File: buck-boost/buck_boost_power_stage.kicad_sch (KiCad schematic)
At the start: 27 parts, among them K1 Relay_SPDT, K2 Relay_SPDT, Q1 Q_NMOS_GDS, Q2 Q_NMOS_GDS, Q3 Q_NMOS_GDS, Q4 Q_NMOS_GDS, Q5 Q_NMOS_GDS

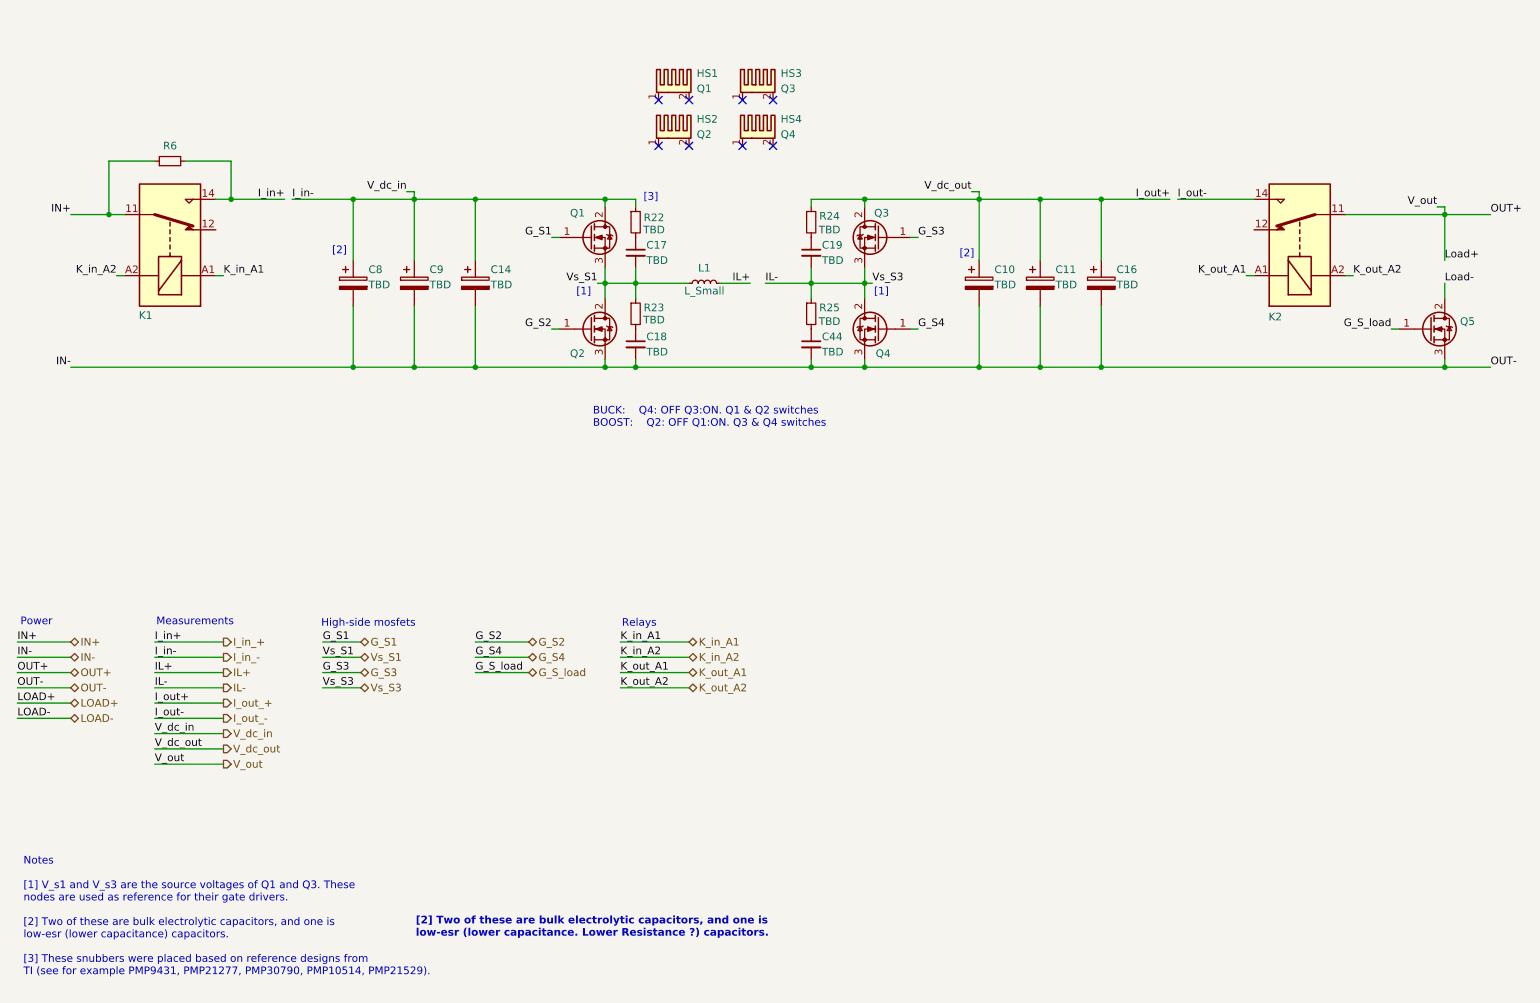
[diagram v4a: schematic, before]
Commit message: Editing sheets(Power labels, sheet color, adding text), Adding information in the sensor sheets
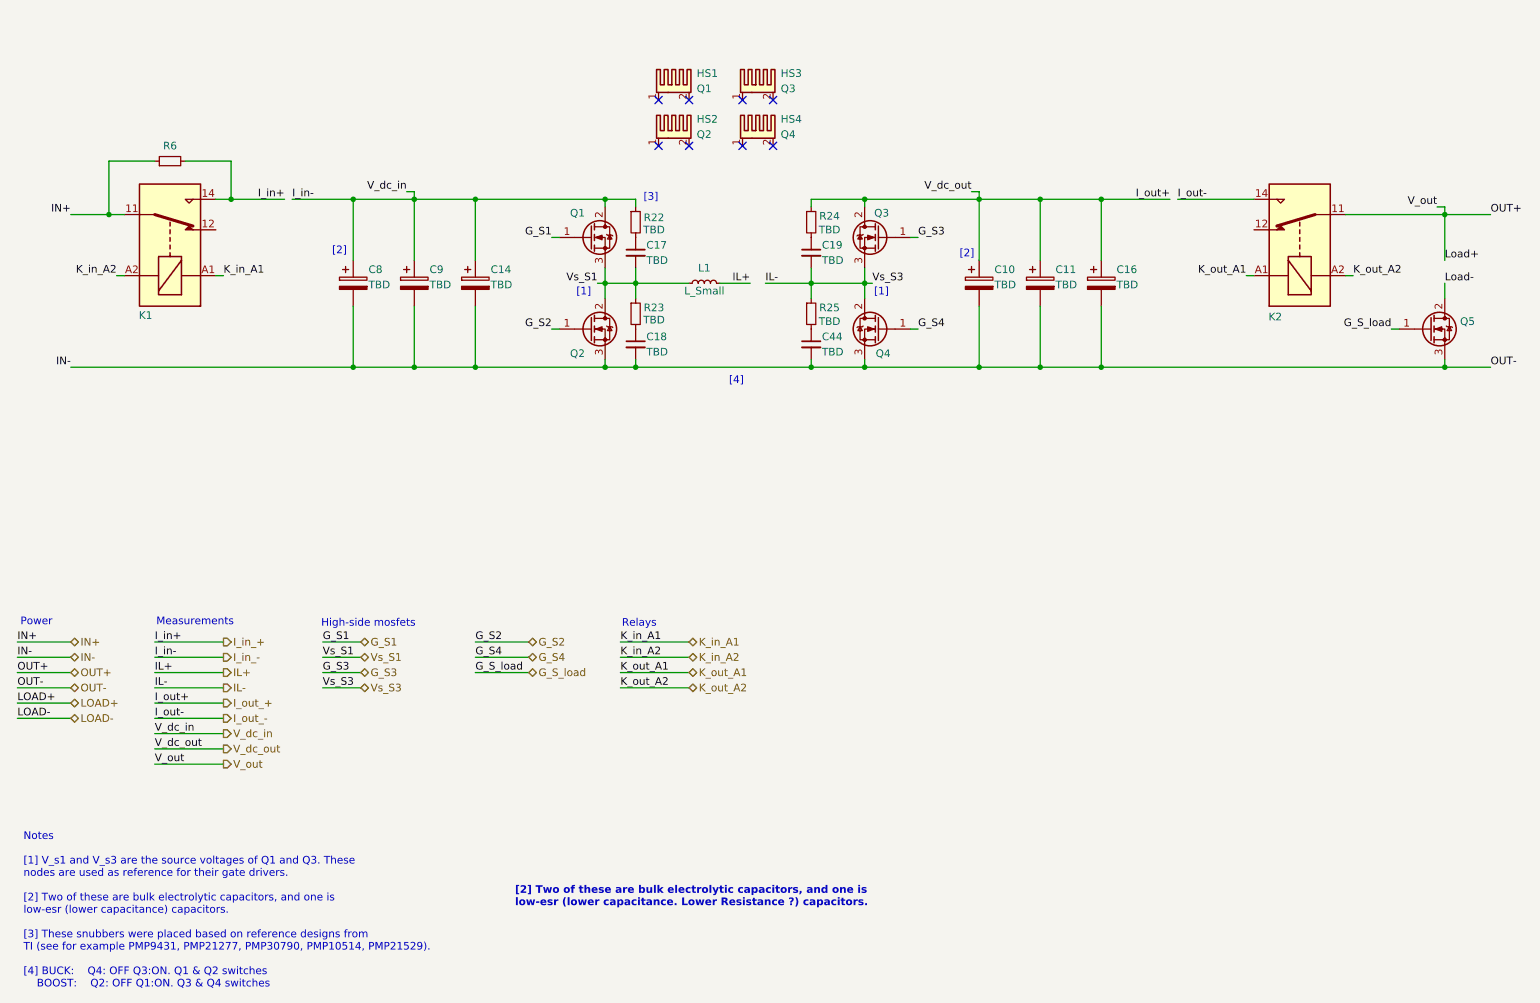
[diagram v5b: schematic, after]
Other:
- note added: "Notes [1] V_s1 and V_s3 are the source voltages of Q1 and Q3. These nodes are used as reference for their gate drivers. [2] Two of these are bulk electrolytic capacitors, and one is low-esr (lower capacitance) capacitors. [3] These snubbers were placed based on reference designs from TI (see for example PMP9431, PMP21277, PMP30790, PMP10514, PMP21529). [4] BUCK: Q4: OFF Q3:ON. Q1 & Q2 switches BO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"
- note added: "[4]"
- note removed: "BUCK: Q4: OFF Q3:ON. Q1 & Q2 switches BOOST: Q2: OFF Q1:ON. Q3 & Q4 switches"
- note removed: "Notes [1] V_s1 and V_s3 are the source voltages of Q1 and Q3. These nodes are used as reference for their gate drivers. [2] Two of these are bulk electrolytic capacitors, and one is low-esr (lower capacitance) capacitors. [3] These snubbers were placed based on reference designs from TI (see for example PMP9431, PMP21277, PMP30790, PMP10514, PMP21529)."
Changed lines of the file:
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@@
 		)
 	)
-	(text "BUCK:	Q4: OFF Q3:ON. Q1 & Q2 switches\nBOOST:	Q2: OFF Q1:ON. Q3 & Q4 switches\n"
-		(exclude_from_sim no)
-		(at 112.268 82.042 0)
-		(effects
-			(font
-				(size 1.27 1.27)
-			)
-			(justify left)
-		)
-	)
-	(text "Notes\n\n[1] V_s1 and V_s3 are the source voltages of Q1 and Q3. These \nnodes are used as reference for their gate drivers.\n\n[2] Two of these are bulk electrolytic capacitors, and one is\nlow-esr (lower capacitance) capacitors.\n\n[3] These snubbers were placed based on reference designs from \nTI (see for example PMP9431, PMP21277, PMP30790, PMP10514, PMP21529)."
+	(text "Notes\n\n[1] V_s1 and V_s3 are the source voltages of Q1 and Q3. These \nnodes are used as reference for their gate drivers.\n\n[2] Two of these are bulk electrolytic capacitors, and one is\nlow-esr (lower capacitance) capacitors.\n\n[3] These snubbers were placed based on reference designs from \nTI (see for example PMP9431, PMP21277, PMP30790, PMP10514, PMP21529).\n\n[4] BUCK:	Q4: OFF Q3:ON. Q1 & Q2 switches\n	BOOST:	Q2: OFF Q1:ON. Q3 & Q4 switches\n "
 		(exclude_from_sim no)
 		(at 17.526 165.1 0)
@@
 	(text "[2] Two of these are bulk electrolytic capacitors, and one is\nlow-esr (lower capacitance. Lower Resistance ?) capacitors."
 		(exclude_from_sim no)
-		(at 82.804 166.878 0)
+		(at 99.314 161.798 0)
 		(effects
 			(font
@@
 		)
 	)
+	(text "[4]"
+		(exclude_from_sim no)
+		(at 136.144 75.946 0)
+		(effects
+			(font
+				(size 1.27 1.27)
+			)
+		)
+	)

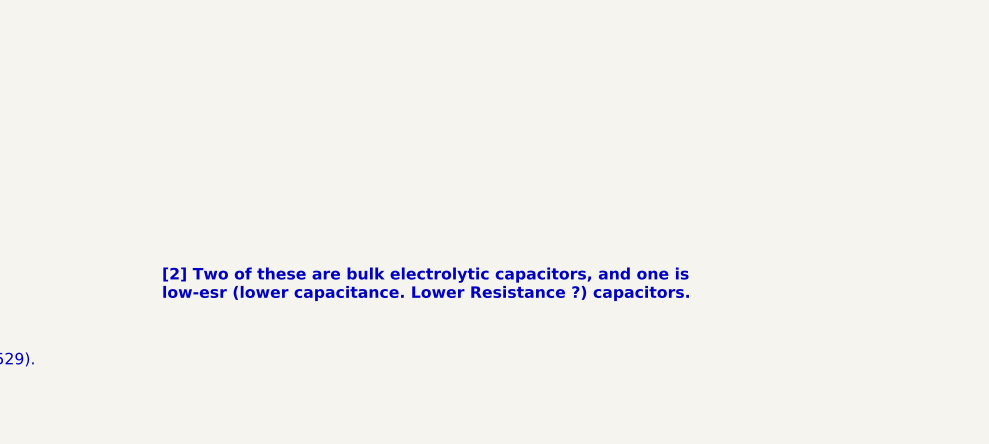
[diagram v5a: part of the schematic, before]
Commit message: Adding supply block
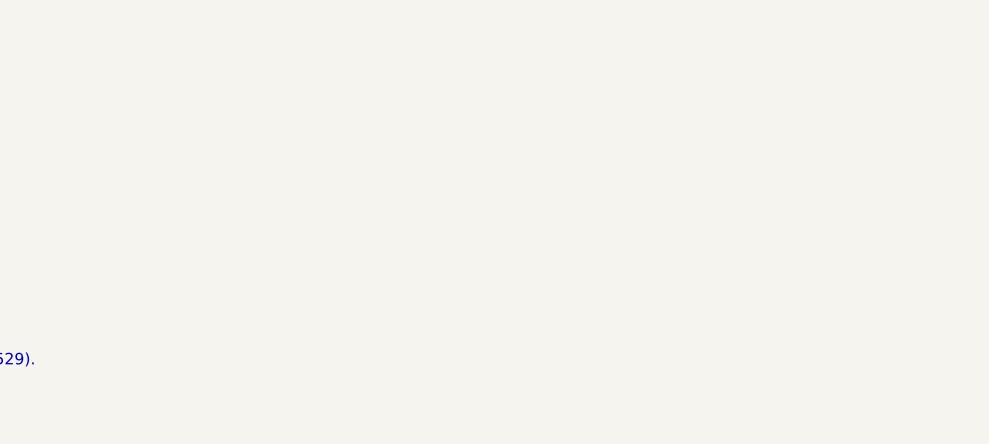
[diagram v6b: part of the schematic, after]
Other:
- note removed: "[2] Two of these are bulk electrolytic capacitors, and one is low-esr (lower capacitance. Lower Resistance ?) capacitors."
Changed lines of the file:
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@@
-		)
-	)
-	(text "[2] Two of these are bulk electrolytic capacitors, and one is\nlow-esr (lower capacitance. Lower Resistance ?) capacitors."
-		(exclude_from_sim no)
-		(at 99.314 161.798 0)
-		(effects
-			(font
-				(size 1.27 1.27)
-				(thickness 0.254)
-				(bold yes)
-				(color 255 0 13 1)
-			)
-			(justify left)
 		)
 	)

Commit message: The changes indicated in the text document Review. 05.11.2024 were implemented. Missing footprints were added
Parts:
- C17, C18, C19, C44: footprint Capacitor_SMD:C_0805_2012Metric_Pad1.18x1.45mm_HandSolder -> Capacitor_SMD:C_1206_3216Metric_Pad1.33x1.80mm_HandSolder
- K1, K2: footprint (none) -> Relay_THT:Relay_SPDT_RAYEX-L90S
- L1: footprint (none) -> CL_Inductor_SMD:L_Bourns_SRP2313AA_24x24
- R22, R23, R24, R25, R6: footprint (none) -> CL_Resistor_SMD:R_MELF_MMB-0207_HandSoldering
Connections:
- net Load- is gone; now on net LOAD-: Q5.2 (D)
- net OUT+ is gone; now on net LOAD+: K2.11
- no-connect marks 8 -> 10
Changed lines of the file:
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@@
 	)
 	(no_connect
+		(at 49.53 50.8)
+	)
+	(no_connect
 		(at 137.16 36.83)
 	)
 	(no_connect
+		(at 222.25 50.8)
+	)
+	(no_connect
 		(at 123.19 36.83)
 	)
@@
 	(wire
 		(pts
+			(xy 254 59.69) (xy 254 62.23)
+		)
+		(stroke
+			(width 0)
+			(type default)
+		)
+	)
+	(wire
+		(pts
 			(xy 119.38 73.66) (xy 148.59 73.66)
 		)
@@
 	(wire
 		(pts
+			(xy 16.51 129.54) (xy 25.4 129.54)
+		)
+		(stroke
+			(width 0)
+			(type default)
+		)
+	)
+	(wire
+		(pts
 			(xy 92.71 45.72) (xy 82.55 45.72)
 		)
@@
 	(wire
 		(pts
+			(xy 16.51 132.08) (xy 25.4 132.08)
+		)
+		(stroke
+			(width 0)
+			(type default)
+		)
+	)
+	(wire
+		(pts
 			(xy 119.38 45.72) (xy 114.3 45.72)
 		)
@@
 	(wire
 		(pts
-			(xy 25.4 129.54) (xy 16.51 129.54)
-		)
-		(stroke
-			(width 0)
-			(type default)
-		)
-	)
-	(wire
-		(pts
 			(xy 116.84 127) (xy 128.27 127)
 		)
@@
 	(wire
 		(pts
-			(xy 254 59.69) (xy 254 62.23)
-		)
-		(stroke
-			(width 0)
-			(type default)
-		)
-	)
-	(wire
-		(pts
 			(xy 50.8 127) (xy 39.37 127)
 		)
@@
 	(wire
 		(pts
-			(xy 25.4 132.08) (xy 16.51 132.08)
-		)
-		(stroke
-			(width 0)
-			(type default)
-		)
-	)
-	(wire
-		(pts
 			(xy 196.85 45.72) (xy 196.85 55.88)
 		)
@@
 		)
 	)
-	(text "Notes\n\n[1] V_s1 and V_s3 are the source voltages of Q1 and Q3. These \nnodes are used as reference for their gate drivers.\n\n[2] Two of these are bulk electrolytic capacitors, and one is\nlow-esr (lower capacitance) capacitors.\n\n[3] These snubbers were placed based on reference designs from \nTI (see for example PMP9431, PMP21277, PMP30790, PMP10514, PMP21529).\n\n[4] BUCK:	Q4: OFF Q3:ON. Q1 & Q2 switches\n	BOOST:	Q2: OFF Q1:ON. Q3 & Q4 switches\n "
+	(text "Notes\n\n[1] V_s1 and V_s3 are the source voltages of Q1 and Q3. These \nnodes are used as reference for their gate drivers.\n\n[2] Two of these are bulk electrolytic capacitors, and one is\nlow-esr (lower capacitance) capacitors.\n\n[3] These snubbers were placed based on reference designs from \nTI (see for example PMP9431, PMP21277, PMP30790, PMP10514, PMP21529).\n\n[4] BUCK:	Q4: OFF Q3:ON. Q1 & Q2 switches\nBOOST:	Q2: OFF Q1:ON. Q3 & Q4 switches\n "
 		(exclude_from_sim no)
 		(at 17.526 165.1 0)
@@
 		)
 	)
-	(label "OUT+"
-		(at 16.51 124.46 0)
+	(label "OUT-"
+		(at 16.51 127 0)
 		(fields_autoplaced yes)
 		(effects
@@
 		)
 	)
-	(label "LOAD+"
-		(at 16.51 129.54 0)
-		(fields_autoplaced yes)
-		(effects
-			(font
-				(size 1.27 1.27)
-			)
-			(justify left bottom)
-		)
-	)
 	(label "I_out+"
 		(at 39.37 129.54 0)
@@
 		)
 	)
+	(label "OUT+"
+		(at 16.51 124.46 0)
+		(fields_autoplaced yes)
+		(effects
+			(font
+				(size 1.27 1.27)
+			)
+			(justify left bottom)
+		)
+	)
 	(label "V_dc_in"
 		(at 39.37 134.62 0)
@@
 		)
 	)
+	(label "Load+"
+		(at 16.51 129.54 0)
+		(fields_autoplaced yes)
+		(effects
+			(font
+				(size 1.27 1.27)
+			)
+			(justify left bottom)
+		)
+	)
 	(label "OUT-"
 		(at 261.62 73.66 0)
@@
 		)
 	)
-	(label "I_in-"
-		(at 39.37 121.92 0)
+	(label "Load-"
+		(at 16.51 132.08 0)
 		(fields_autoplaced yes)
 		(effects
@@
 		)
 	)
-	(label "G_S3"
-		(at 67.31 124.46 0)
+	(label "I_in-"
+		(at 39.37 121.92 0)
 		(fields_autoplaced yes)
 		(effects
@@
 		)
 	)
-	(label "OUT-"
-		(at 16.51 127 0)
+	(label "G_S3"
+		(at 67.31 124.46 0)
 		(fields_autoplaced yes)
 		(effects
@@
 		)
 	)
-	(label "LOAD-"
-		(at 16.51 132.08 0)
-		(fields_autoplaced yes)
-		(effects
-			(font
-				(size 1.27 1.27)
-			)
-			(justify left bottom)
-		)
-	)
 	(label "IN-"
 		(at 16.51 121.92 0)
@@
 			)
 		)
-		(property "Footprint" "Capacitor_SMD:C_0805_2012Metric_Pad1.18x1.45mm_HandSolder"
+		(property "Footprint" "Capacitor_SMD:C_1206_3216Metric_Pad1.33x1.80mm_HandSolder"
 			(at 148.59 54.61 0)
 			(effects
@@
 			)
 		)
-		(property "Footprint" "Capacitor_SMD:C_0805_2012Metric_Pad1.18x1.45mm_HandSolder"
+		(property "Footprint" "Capacitor_SMD:C_1206_3216Metric_Pad1.33x1.80mm_HandSolder"
 			(at 119.38 54.61 0)
 			(effects
@@
 			)
 		)
-		(property "Footprint" ""
+		(property "Footprint" "CL_Resistor_SMD:R_MELF_MMB-0207_HandSoldering"
 			(at 148.59 64.77 0)
 			(effects
@@
 			)
 		)
-		(property "Footprint" ""
+		(property "Footprint" "CL_Resistor_SMD:R_MELF_MMB-0207_HandSoldering"
 			(at 148.59 49.53 0)
 			(effects
@@
 			)
 		)
-		(property "Footprint" ""
+		(property "Footprint" "CL_Resistor_SMD:R_MELF_MMB-0207_HandSoldering"
 			(at 41.91 39.37 0)
 			(effects
@@
 			)
 		)
-		(property "Footprint" "Capacitor_SMD:C_0805_2012Metric_Pad1.18x1.45mm_HandSolder"
+		(property "Footprint" "Capacitor_SMD:C_1206_3216Metric_Pad1.33x1.80mm_HandSolder"
 			(at 119.38 69.85 0)
 			(effects
@@
 			)
 		)
-		(property "Footprint" ""
+		(property "Footprint" "CL_Resistor_SMD:R_MELF_MMB-0207_HandSoldering"
 			(at 119.38 64.77 0)
 			(effects
@@
 			)
 		)
-		(property "Footprint" ""
+		(property "Footprint" "Relay_THT:Relay_SPDT_RAYEX-L90S"
 			(at 231.14 41.91 0)
 			(effects
@@
 			)
 		)
-		(property "Footprint" ""
+		(property "Footprint" "Relay_THT:Relay_SPDT_RAYEX-L90S"
 			(at 40.64 41.91 0)
 			(effects
@@
 			)
 		)
-		(property "Footprint" ""
+		(property "Footprint" "CL_Resistor_SMD:R_MELF_MMB-0207_HandSoldering"
 			(at 119.38 49.53 0)
 			(effects
@@
 			)
 		)
-		(property "Footprint" ""
+		(property "Footprint" "CL_Inductor_SMD:L_Bourns_SRP2313AA_24x24"
 			(at 130.81 59.69 0)
 			(effects
@@
 			)
 		)
-		(property "Footprint" "Capacitor_SMD:C_0805_2012Metric_Pad1.18x1.45mm_HandSolder"
+		(property "Footprint" "Capacitor_SMD:C_1206_3216Metric_Pad1.33x1.80mm_HandSolder"
 			(at 148.59 69.85 0)
 			(effects

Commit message: Some errors in the schematics were corrected. PCB file V1.0
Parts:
- HS1, HS2, HS3, HS4: footprint Heatsink:Heatsink_Stonecold_HS-132_32x14mm_2xFixation1.5mm -> CL_Heatsink:Heatsink_Stonecold_HS-132_32x14mm_2xFixation1.5mm_2pins
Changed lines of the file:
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@@
 			)
 		)
-		(property "Footprint" "Heatsink:Heatsink_Stonecold_HS-132_32x14mm_2xFixation1.5mm"
+		(property "Footprint" "CL_Heatsink:Heatsink_Stonecold_HS-132_32x14mm_2xFixation1.5mm_2pins"
 			(at 126.0348 35.56 0)
 			(effects
@@
 			)
 		)
-		(property "Footprint" "Heatsink:Heatsink_Stonecold_HS-132_32x14mm_2xFixation1.5mm"
+		(property "Footprint" "CL_Heatsink:Heatsink_Stonecold_HS-132_32x14mm_2xFixation1.5mm_2pins"
 			(at 140.0048 35.56 0)
 			(effects
@@
 			)
 		)
-		(property "Footprint" "Heatsink:Heatsink_Stonecold_HS-132_32x14mm_2xFixation1.5mm"
+		(property "Footprint" "CL_Heatsink:Heatsink_Stonecold_HS-132_32x14mm_2xFixation1.5mm_2pins"
 			(at 140.0048 27.94 0)
 			(effects
@@
 			)
 		)
-		(property "Footprint" "Heatsink:Heatsink_Stonecold_HS-132_32x14mm_2xFixation1.5mm"
+		(property "Footprint" "CL_Heatsink:Heatsink_Stonecold_HS-132_32x14mm_2xFixation1.5mm_2pins"
 			(at 126.0348 27.94 0)
 			(effects
